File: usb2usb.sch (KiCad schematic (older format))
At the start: 32 parts, among them J1 USB_B, J2 USB_A, SW1 PUSH, U1 ATMEGA32U4, U2 MIC5504, U3 MAX3421E, X1 8/16MHz, X2 12MHz

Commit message: Fix power pin of USB connector
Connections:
- wire segments 142 -> 141
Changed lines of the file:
@@
 P 8450 3550
 F 0 "J2" H 8050 3550 60  0000 C CNN
-F 1 "USB_A" H 8300 3800 60  0001 C CNN
+F 1 "USB_A" H 8300 3200 60  0000 C CNN
 F 2 "" H 8450 3550 60  0000 C CNN
 F 3 "" H 8450 3550 60  0000 C CNN
@@
 P 2100 1650
 F 0 "J1" H 1700 1650 60  0000 C CNN
-F 1 "USB_B" H 1950 1900 60  0001 C CNN
+F 1 "USB_B" H 1950 1900 60  0000 C CNN
 F 2 "" H 2100 1650 60  0000 C CNN
 F 3 "" H 2100 1650 60  0000 C CNN
@@
 	1    0    0    -1
 $EndComp
-$Comp
-L PWR_FLAG #FLG021
-U 1 1 5498E0F6
-P 10900 2900
-F 0 "#FLG021" H 10900 2995 30  0001 C CNN
-F 1 "PWR_FLAG" H 10900 3080 30  0000 C CNN
-F 2 "" H 10900 2900 60  0000 C CNN
-F 3 "" H 10900 2900 60  0000 C CNN
-	1    10900 2900
-	1    0    0    -1
-$EndComp
-$Comp
-L GND #PWR022
-U 1 1 5498E12A
-P 10900 2950
-F 0 "#PWR022" H 10900 2700 60  0001 C CNN
-F 1 "GND" H 10900 2800 60  0000 C CNN
-F 2 "" H 10900 2950 60  0000 C CNN
-F 3 "" H 10900 2950 60  0000 C CNN
-	1    10900 2950
-	1    0    0    -1
-$EndComp
-Wire Wire Line
-	10900 2900 10900 2950
 Text Notes 2500 1850 0    60   ~ 0
 To host

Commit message: Rev.A
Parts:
- removed C13: 1u, symbol C
- removed C8, C9: 0.1u, symbol C
- removed R1: 10K, symbol R
- removed R5: 1K, symbol R
- added C1: 1u, Capacitors_SMD:C_0603_HandSoldering, symbol C
- C10: renamed from C14; value 18pF -> 18p; footprint (none) -> Capacitors_SMD:C_0603_HandSoldering
- C11: renamed from C15; value 18pF -> 18p; footprint (none) -> Capacitors_SMD:C_0603_HandSoldering
- C12: renamed from C4; footprint (none) -> Capacitors_SMD:C_0603_HandSoldering
- C13: renamed from C5; footprint (none) -> Capacitors_SMD:C_0603_HandSoldering
- C2: renamed from C1; footprint (none) -> Capacitors_SMD:C_0603_HandSoldering
- C3: renamed from C7; footprint (none) -> Capacitors_SMD:C_0603_HandSoldering
- C4: renamed from C2; footprint (none) -> Capacitors_SMD:C_0603_HandSoldering
- C5: renamed from C3; footprint (none) -> Capacitors_SMD:C_0603_HandSoldering
- C6: footprint (none) -> Capacitors_SMD:C_0603_HandSoldering
- C7: renamed from C12; footprint (none) -> Capacitors_SMD:C_0603_HandSoldering
- C8: renamed from C10; footprint (none) -> Capacitors_SMD:C_1206_HandSoldering
- C9: renamed from C11; value 1u -> 0.1u; footprint (none) -> Capacitors_SMD:C_0603_HandSoldering
- D1: footprint (none) -> keyboard:LED_2012_HSOL
- J1: footprint (none) -> keyboard:USB_A_PLUG
- J2: footprint (none) -> Connect:USB_A
- R1: renamed from R2; footprint (none) -> Resistors_SMD:R_0603_HandSoldering
- R2: renamed from R3; footprint (none) -> Resistors_SMD:R_0603_HandSoldering
- R3: renamed from R4; footprint (none) -> Resistors_SMD:R_0603_HandSoldering
- R4: renamed from R6; footprint (none) -> Resistors_SMD:R_0603_HandSoldering
- R5: renamed from R7; footprint (none) -> Resistors_SMD:R_0603_HandSoldering
- R6: renamed from R8; footprint (none) -> Resistors_SMD:R_0603_HandSoldering
- SW1: footprint (none) -> keyboard:SW_ALPS_SKRP
- U1: footprint (none) -> Housings_QFP:LQFP-44_10x10mm_Pitch0.8mm
- U2: renamed from U3; footprint (none) -> Housings_QFP:LQFP-32_5x5mm_Pitch0.5mm
- U3: renamed from U2; value MIC5504 -> MIC5504-3.3; footprint (none) -> Housings_SOT-23_SOT-143_TSOT-6:SC70-6_Handsoldering
- X1: value 8/16MHz -> 16MHz; footprint (none) -> Crystals_Oscillators_SMD:crystal_FA238-TSX3225
- X2: footprint (none) -> Crystals_Oscillators_SMD:crystal_FA238-TSX3225
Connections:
- net labels added: INT
- net labels removed: GPX
- wire segments 141 -> 128
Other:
- note added: "33ohm on D+/D-\nrequire 1%"
- note added: "Optional:\npull-up resistor for reset"
- note removed: "33ohm on D+/D- require 1%"
- note removed: "Optional?"
- moved on the sheet: C12, C13, C3, C6, SW1, U3

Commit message: Update footprint with rounded pads
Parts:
- C1, C10, C11, C12, C13, C2, C3, C4, C5, C6, C7, C8, C9: symbol C -> keyboard_parts:C
- D1: symbol LED -> Device:LED
- J1: symbol USB_B -> keyboard_parts:USB_B
- J2: symbol USB_A -> keyboard_parts:USB_A
- R1, R2, R3, R4, R5, R6: symbol R -> keyboard_parts:R
- SW1: symbol SW_PUSH -> keyboard_parts:SW_PUSH
- U1: symbol ATMEGA32U4 -> keyboard_parts:ATMEGA32U4
- U2: symbol MAX3421E -> keyboard_parts:MAX3421E
- U3: symbol LDO_REGULATOR -> keyboard_parts:LDO_REGULATOR
- X1, X2: symbol CRYSTAL -> keyboard_parts:XTAL_GND
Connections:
- wire segments 128 -> 161

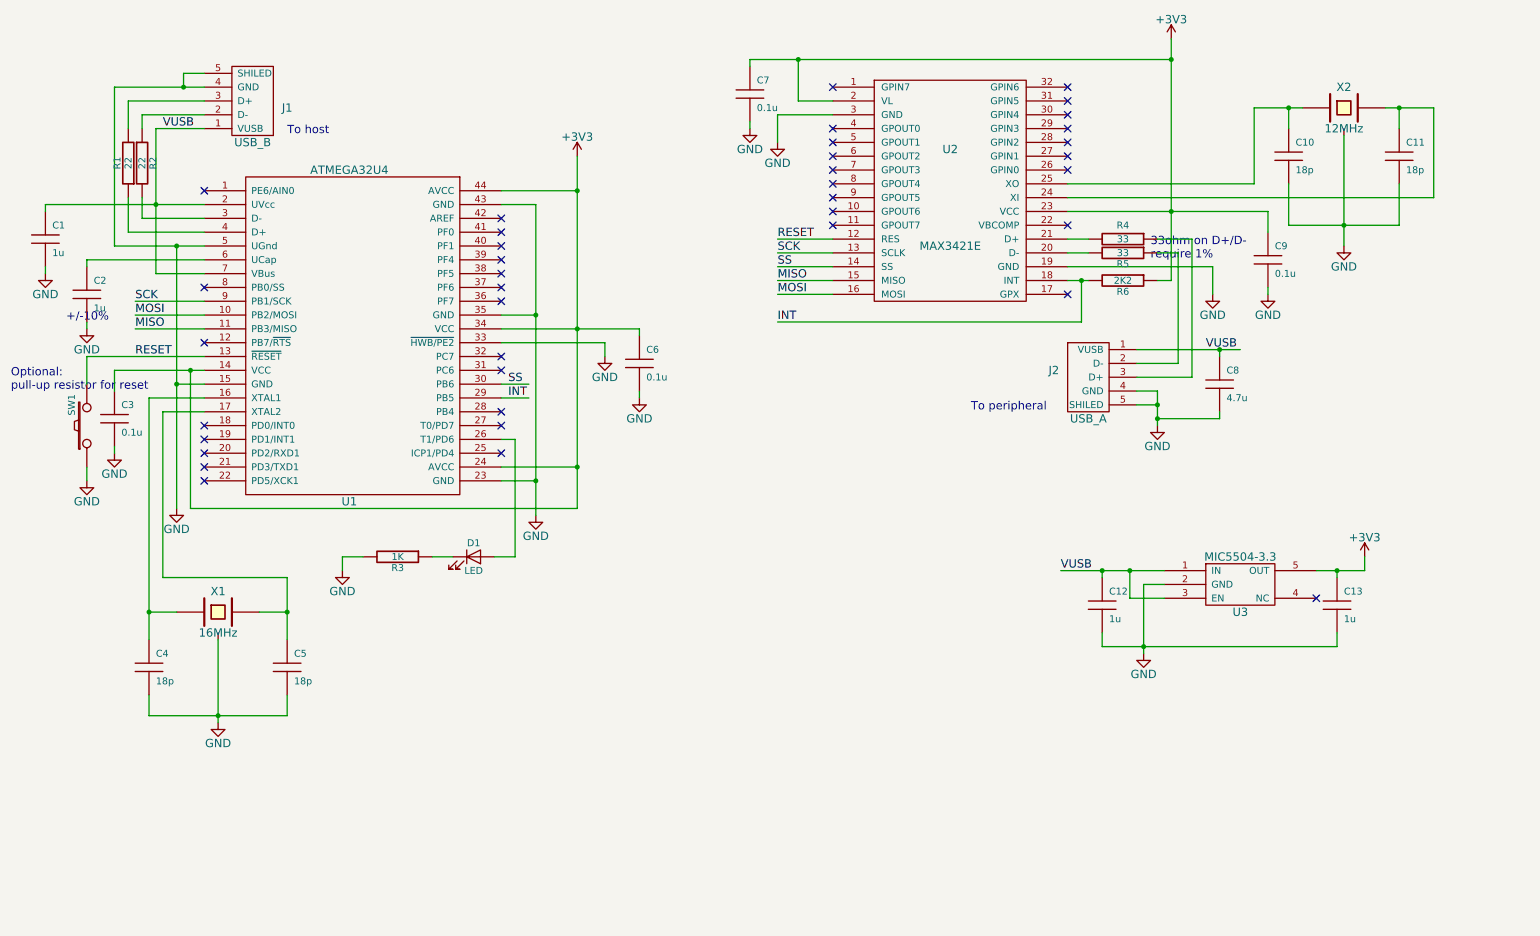
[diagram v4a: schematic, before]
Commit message: Remove LED
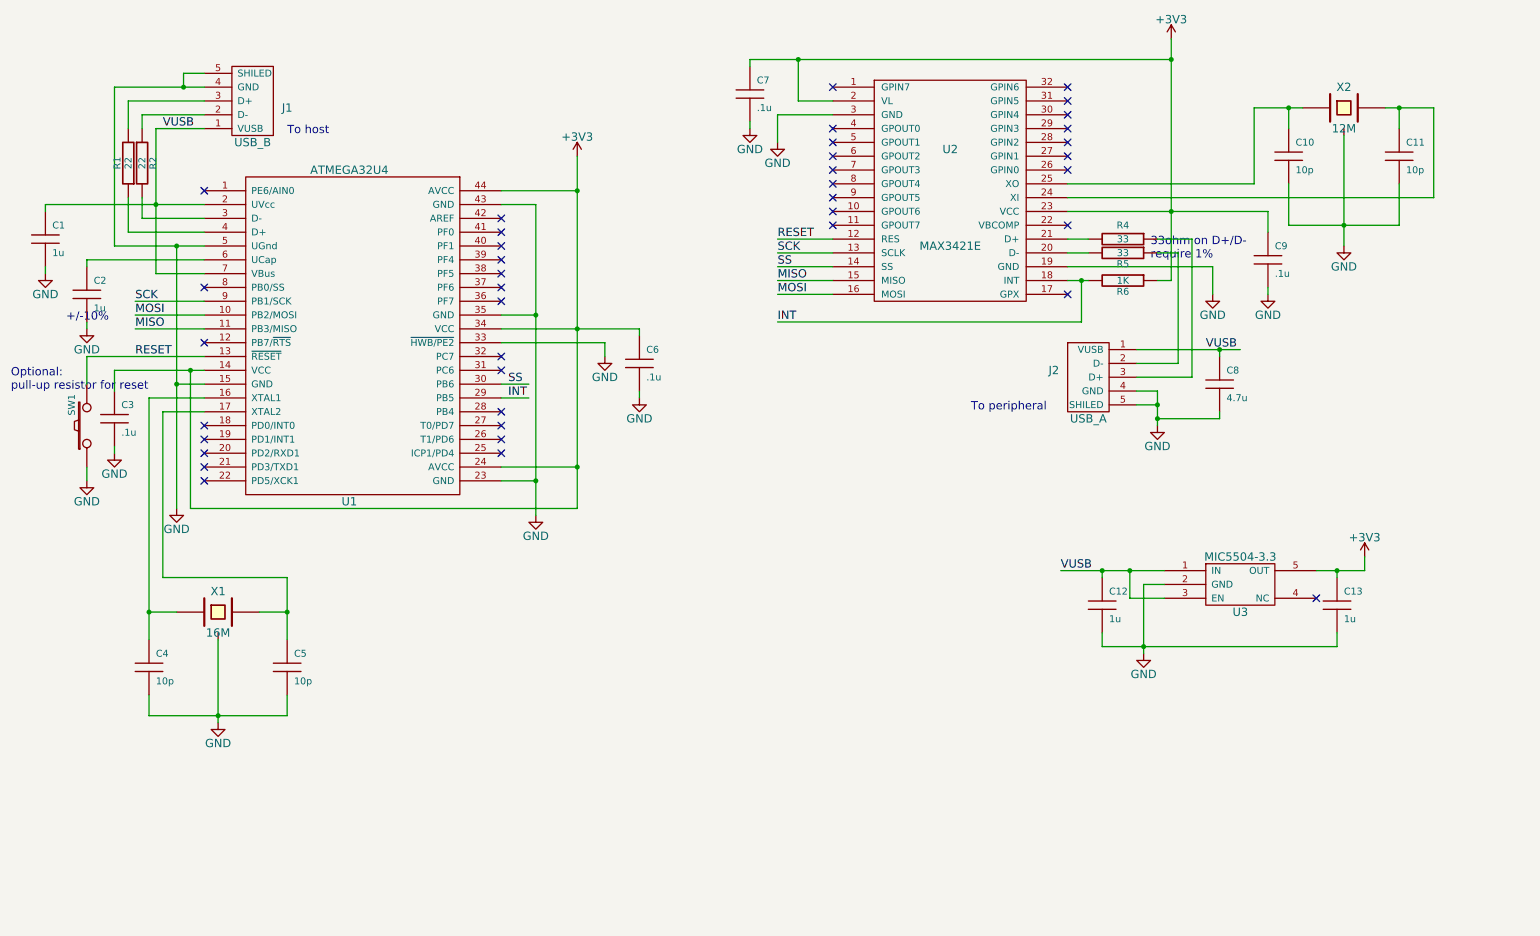
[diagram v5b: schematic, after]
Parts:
- removed D1: LED, keyboard:LED_2012_HSOL, symbol Device:LED
- removed R3: 1K, Resistors_SMD:R_0603_HandSoldering, symbol keyboard_parts:R
- C10, C11, C4, C5: value 18p -> 10p
- C3, C6, C7, C9: value 0.1u -> .1u
- R6: value 2K2 -> 1K
- X1: value 16MHz -> 16M
- X2: value 12MHz -> 12M
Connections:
- no-connect marks 39 -> 40
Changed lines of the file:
@@
 EESchema Schematic File Version 4
-LIBS:usb2usb-cache
-EELAYER 29 0
+EELAYER 30 0
 EELAYER END
 $Descr A4 11693 8268
@@
 P 10150 1650
 F 0 "X2" H 10150 1800 60  0000 C CNN
-F 1 "12MHz" H 10150 1500 60  0000 C CNN
+F 1 "12M" H 10150 1500 60  0000 C CNN
 F 2 "Crystals_Oscillators_SMD:crystal_FA238-TSX3225" H 10150 1650 60  0001 C CNN
 F 3 "" H 10150 1650 60  0000 C CNN
@@
 P 10550 2000
 F 0 "C11" H 10600 2100 50  0000 L CNN
-F 1 "18p" H 10600 1900 50  0000 L CNN
+F 1 "10p" H 10600 1900 50  0000 L CNN
 F 2 "Capacitors_SMD:C_0603_HandSoldering" H 10550 2000 60  0001 C CNN
 F 3 "" H 10550 2000 60  0000 C CNN
@@
 P 9750 2000
 F 0 "C10" H 9800 2100 50  0000 L CNN
-F 1 "18p" H 9800 1900 50  0000 L CNN
+F 1 "10p" H 9800 1900 50  0000 L CNN
 F 2 "Capacitors_SMD:C_0603_HandSoldering" H 9750 2000 60  0001 C CNN
 F 3 "" H 9750 2000 60  0000 C CNN
@@
 P 8550 2900
 F 0 "R6" V 8630 2900 50  0000 C CNN
-F 1 "2K2" V 8550 2900 50  0000 C CNN
+F 1 "1K" V 8550 2900 50  0000 C CNN
 F 2 "Resistors_SMD:R_0603_HandSoldering" H 8550 2900 60  0001 C CNN
 F 3 "" H 8550 2900 60  0000 C CNN
@@
 P 2000 5300
 F 0 "X1" H 2000 5450 60  0000 C CNN
-F 1 "16MHz" H 2000 5150 60  0000 C CNN
+F 1 "16M" H 2000 5150 60  0000 C CNN
 F 2 "Crystals_Oscillators_SMD:crystal_FA238-TSX3225" H 2000 5300 60  0001 C CNN
 F 3 "" H 2000 5300 60  0000 C CNN
@@
 P 2500 5700
 F 0 "C5" H 2550 5800 50  0000 L CNN
-F 1 "18p" H 2550 5600 50  0000 L CNN
+F 1 "10p" H 2550 5600 50  0000 L CNN
 F 2 "Capacitors_SMD:C_0603_HandSoldering" H 2500 5700 60  0001 C CNN
 F 3 "" H 2500 5700 60  0000 C CNN
@@
 P 1500 5700
 F 0 "C4" H 1550 5800 50  0000 L CNN
-F 1 "18p" H 1550 5600 50  0000 L CNN
+F 1 "10p" H 1550 5600 50  0000 L CNN
 F 2 "Capacitors_SMD:C_0603_HandSoldering" H 1500 5700 60  0001 C CNN
 F 3 "" H 1500 5700 60  0000 C CNN
@@
 $EndComp
 NoConn ~ 1900 2250
-$Comp
-L keyboard_parts:R R3
-U 1 1 549794FF
-P 3300 4900
-F 0 "R3" V 3380 4900 50  0000 C CNN
-F 1 "1K" V 3300 4900 50  0000 C CNN
-F 2 "Resistors_SMD:R_0603_HandSoldering" H 3300 4900 60  0001 C CNN
-F 3 "" H 3300 4900 60  0000 C CNN
-	1    3300 4900
-	0    1    1    0
-$EndComp
-$Comp
-L Device:LED D1
-U 1 1 5497957F
-P 3850 4900
-F 0 "D1" H 3850 5000 50  0000 C CNN
-F 1 "LED" H 3850 4800 50  0000 C CNN
-F 2 "keyboard:LED_2012_HSOL" H 3850 4900 60  0001 C CNN
-F 3 "" H 3850 4900 60  0000 C CNN
-	1    3850 4900
-	1    0    0    -1
-$EndComp
-$Comp
-L power:GND #PWR011
-U 1 1 54979D14
-P 2900 5000
-F 0 "#PWR011" H 2900 4750 60  0001 C CNN
-F 1 "GND" H 2900 4850 60  0000 C CNN
-F 2 "" H 2900 5000 60  0000 C CNN
-F 3 "" H 2900 5000 60  0000 C CNN
-	1    2900 5000
-	1    0    0    -1
-$EndComp
 NoConn ~ 4050 4150
 $Comp
@@
 P 5050 3500
 F 0 "C6" H 5100 3600 50  0000 L CNN
-F 1 "0.1u" H 5100 3400 50  0000 L CNN
+F 1 ".1u" H 5100 3400 50  0000 L CNN
 F 2 "Capacitors_SMD:C_0603_HandSoldering" H 5050 3500 60  0001 C CNN
 F 3 "" H 5050 3500 60  0000 C CNN
@@
 P 1250 3900
 F 0 "C3" H 1300 4000 50  0000 L CNN
-F 1 "0.1u" H 1300 3800 50  0000 L CNN
+F 1 ".1u" H 1300 3800 50  0000 L CNN
 F 2 "Capacitors_SMD:C_0603_HandSoldering" H 1250 3900 60  0001 C CNN
 F 3 "" H 1250 3900 60  0000 C CNN
@@
 MISO
 $Comp
-L keyboard_parts:C C7
-U 1 1 54983857
-P 5850 1550
-F 0 "C7" H 5900 1650 50  0000 L CNN
-F 1 "0.1u" H 5900 1450 50  0000 L CNN
-F 2 "Capacitors_SMD:C_0603_HandSoldering" H 5850 1550 60  0001 C CNN
-F 3 "" H 5850 1550 60  0000 C CNN
-	1    5850 1550
-	1    0    0    -1
-$EndComp
-$Comp
 L keyboard_parts:C C9
 U 1 1 54983C9B
 P 9600 2750
 F 0 "C9" H 9650 2850 50  0000 L CNN
-F 1 "0.1u" H 9650 2650 50  0000 L CNN
+F 1 ".1u" H 9650 2650 50  0000 L CNN
 F 2 "Capacitors_SMD:C_0603_HandSoldering" H 9600 2750 60  0001 C CNN
 F 3 "" H 9600 2750 60  0000 C CNN
@@
 	1450 2450 1450 2300
 Wire Wire Line
-	4150 4050 4050 4050
-Wire Wire Line
-	3050 4900 2900 4900
-Wire Wire Line
-	2900 4900 2900 5000
-Wire Wire Line
-	4150 4900 4150 4050
-Wire Wire Line
 	1600 3850 1900 3850
 Wire Wire Line
@@
 Wire Wire Line
 	1700 3650 1700 4550
-Wire Wire Line
-	4000 4900 4150 4900
-Wire Wire Line
-	3550 4900 3700 4900
+NoConn ~ 4050 4050
+$Comp
+L keyboard_parts:C C7
+U 1 1 54983857
+P 5850 1550
+F 0 "C7" H 5900 1650 50  0000 L CNN
+F 1 ".1u" H 5900 1450 50  0000 L CNN
+F 2 "Capacitors_SMD:C_0603_HandSoldering" H 5850 1550 60  0001 C CNN
+F 3 "" H 5850 1550 60  0000 C CNN
+	1    5850 1550
+	1    0    0    -1
+$EndComp
 $EndSCHEMATC
